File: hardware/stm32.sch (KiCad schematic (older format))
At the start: 35 parts, among them J6 PROG, Q1 PMBT3906,215, Q15 AO3400 (A09T), Q16 AO3400 (A09T), Q17 AO3400 (A09T), Q18 AO3400 (A09T), Q19 AO3400 (A09T), Q2 PMBT3906,215, Q20 AO3400 (A09T), Q3 PMBT3906,215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

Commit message: Rev5 schematic changes and pcb cleanup
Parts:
- removed Q1, Q2, Q3, Q4, Q5, Q6, Q7, Q8: PMBT3906,215, Package_TO_SOT_SMD:SOT-23, symbol Device:Q_PNP_BEC
- removed Q15, Q16, Q17, Q18, Q19, Q20: AO3400 (A09T), Package_TO_SOT_SMD:SOT-23, symbol Transistor_FET:DMN2050L
- removed R35, R36, R37, R38, R39, R40, R41, R42: 680, Resistor_SMD:R_0603_1608Metric, symbol Device:R
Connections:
- net labels added: CLK, LE, OE, SDI
- net labels removed: B1, B2, G1, G2, L1, L2, L3, L4, L5, L6, L7, L8, R1, R2, VCC
- wire segments 142 -> 69

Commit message: Finished routing rev5
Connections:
- net CLK: now also U7.26 (PB13)
- net LE: now also U7.25 (PB12)
- net OE: now also U7.27 (PB14)
- net SDI: now also U7.28 (PB15)
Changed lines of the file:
@@
 Text HLabel 4400 4200 0    50   Input ~ 0
 i2c_SDA
-Text HLabel 3650 4850 0    50   Output ~ 0
+Text HLabel 4250 4900 0    50   Output ~ 0
 OE
-Text HLabel 3650 4950 0    50   Output ~ 0
+Text HLabel 4250 4800 0    50   Output ~ 0
 CLK
-Text HLabel 3650 5050 0    50   Output ~ 0
+Text HLabel 4250 4700 0    50   Output ~ 0
+LE
+Wire Wire Line
+	4250 5000 4500 5000
+Text HLabel 4250 5000 0    50   Output ~ 0
 SDI
-Text HLabel 3650 5150 0    50   Output ~ 0
-LE
+Wire Wire Line
+	4250 4800 4500 4800
+Wire Wire Line
+	4500 4700 4250 4700
+Wire Wire Line
+	4250 4900 4500 4900
 $EndSCHEMATC

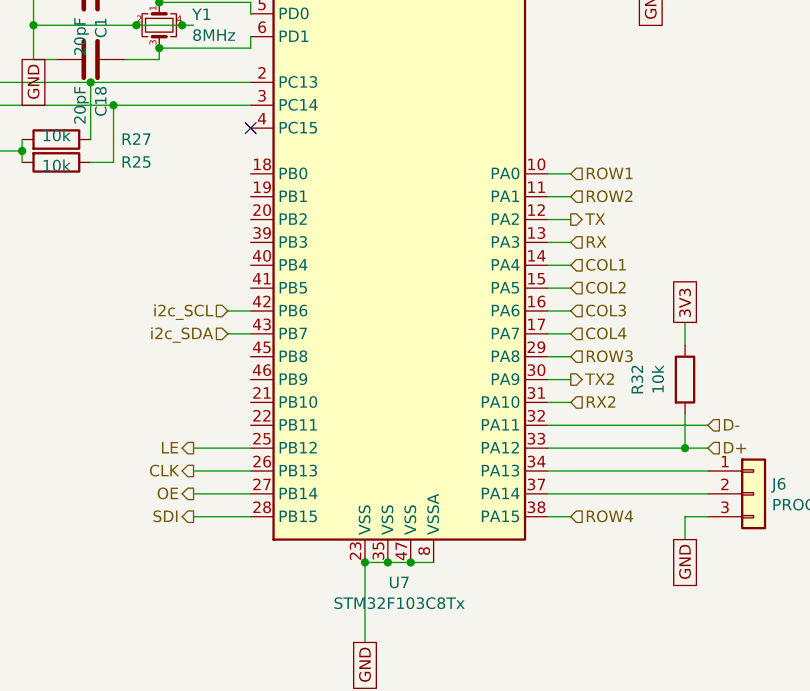
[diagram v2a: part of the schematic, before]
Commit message: UART changes
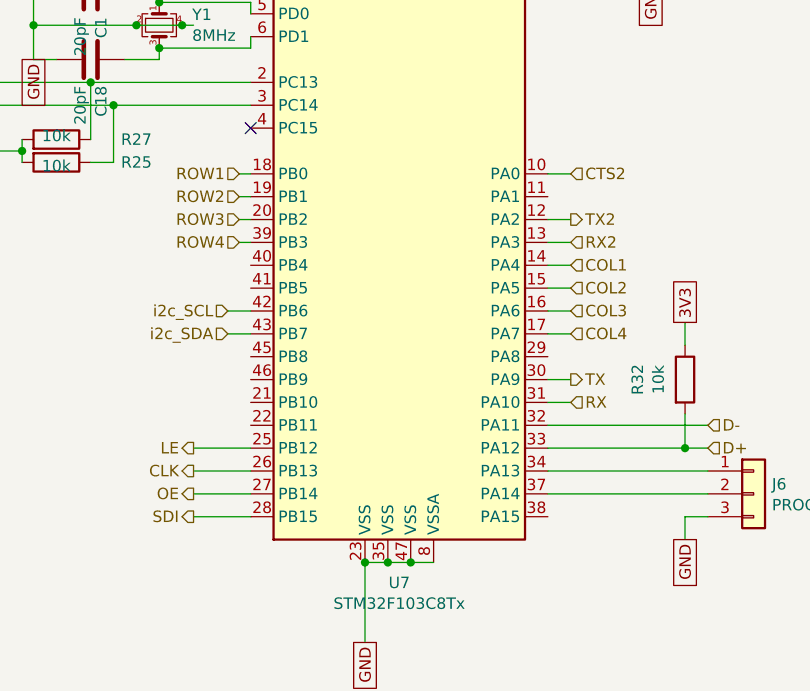
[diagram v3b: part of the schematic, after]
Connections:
- net ROW1: now also U7.18 (PB0); no longer U7.10 (PA0)
- net ROW2: now also U7.19 (PB1); no longer U7.11 (PA1)
- net ROW3: now also U7.20 (PB2); no longer U7.29 (PA8)
- net ROW4: now also U7.39 (PB3); no longer U7.38 (PA15)
- net RX: now also U7.31 (PA10); no longer U7.13 (PA3)
- net RX2: now also U7.13 (PA3); no longer U7.31 (PA10)
- net TX: now also U7.30 (PA9); no longer U7.12 (PA2)
- net TX2: now also U7.12 (PA2); no longer U7.30 (PA9)
- new net CTS2: U7.10 (PA0)
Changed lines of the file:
@@
 	4400 4100 4500 4100
 Text HLabel 5900 3700 2    50   Output ~ 0
-TX
+TX2
 Wire Wire Line
 	5900 3700 5800 3700
 Text HLabel 5900 3800 2    50   Input ~ 0
-RX
+RX2
 Wire Wire Line
 	5900 3800 5800 3800
 Text HLabel 5900 4400 2    50   Output ~ 0
-TX2
+TX
 Wire Wire Line
 	5900 4400 5800 4400
 Text HLabel 5900 4500 2    50   Input ~ 0
-RX2
+RX
 Wire Wire Line
 	5900 4500 5800 4500
-Text HLabel 5900 3500 2    50   Input ~ 0
+Text HLabel 4450 3500 0    50   Input ~ 0
 ROW1
 Text HLabel 5900 3900 2    50   Input ~ 0
@@
 Wire Wire Line
 	5900 4200 5800 4200
-Wire Wire Line
-	5900 3500 5800 3500
-Text HLabel 5900 3600 2    50   Input ~ 0
+Text HLabel 4450 3600 0    50   Input ~ 0
 ROW2
-Wire Wire Line
-	5900 3600 5800 3600
-Text HLabel 5900 4300 2    50   Input ~ 0
+Text HLabel 4450 3700 0    50   Input ~ 0
 ROW3
-Wire Wire Line
-	5900 4300 5800 4300
-Text HLabel 5900 5000 2    50   Input ~ 0
+Text HLabel 4450 3800 0    50   Input ~ 0
 ROW4
-Wire Wire Line
-	5900 5000 5800 5000
 $Comp
 L Device:Crystal_GND24_Small Y1
@@
 Wire Wire Line
 	4250 4900 4500 4900
+Wire Wire Line
+	4450 3500 4500 3500
+Wire Wire Line
+	4450 3600 4500 3600
+Wire Wire Line
+	4450 3700 4500 3700
+Wire Wire Line
+	4450 3800 4500 3800
+Text HLabel 5900 3500 2    50   Input ~ 0
+CTS2
+Wire Wire Line
+	5900 3500 5800 3500
 $EndSCHEMATC

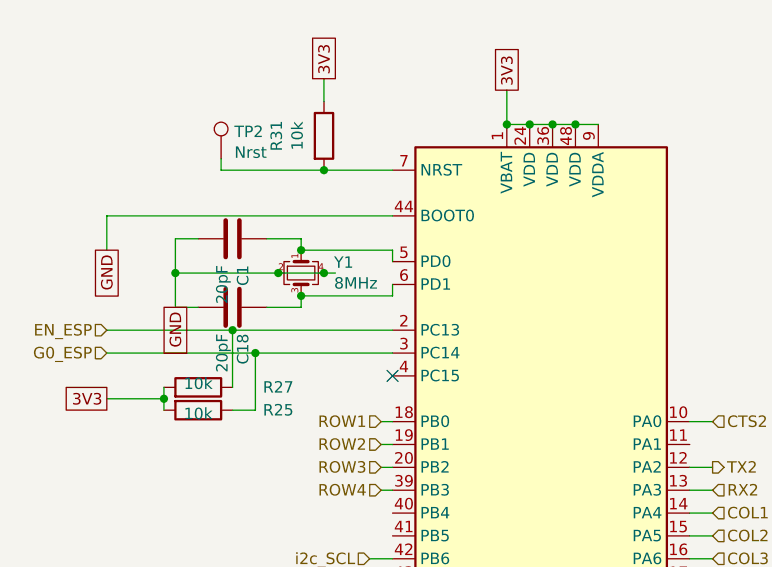
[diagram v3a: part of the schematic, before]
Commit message: Fixed BOM lines
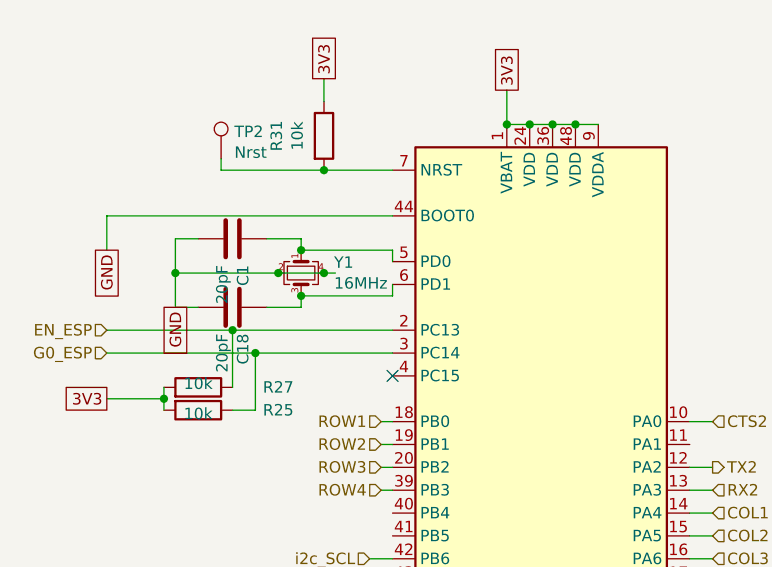
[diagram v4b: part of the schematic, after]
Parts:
- Y1: value 8MHz -> 16MHz; LCSC C280087 -> C13738
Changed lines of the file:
@@
 P 4100 2850
 F 0 "Y1" V 4054 2994 50  0000 L CNN
-F 1 "8MHz" V 4145 2994 50  0000 L CNN
+F 1 "16MHz" V 4145 2994 50  0000 L CNN
 F 2 "Crystal:Crystal_SMD_3225-4Pin_3.2x2.5mm" H 4100 2850 50  0001 C CNN
 F 3 "~" H 4100 2850 50  0001 C CNN
-F 4 "C280087" H 4100 2850 50  0001 C CNN "LCSC"
+F 4 "C13738" H 4100 2850 50  0001 C CNN "LCSC"
 	1    4100 2850
 	0    1    1    0

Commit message: Switch to tag connect for programming header
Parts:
- J6: footprint Connector_PinSocket_2.54mm:PinSocket_1x03_P2.54mm_Vertical_SMD_Pin1Left -> Connector:Tag-Connect_TC2030-IDC-NL_2x03_P1.27mm_Vertical
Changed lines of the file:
@@
 F 0 "J6" H 6780 4942 50  0000 L CNN
 F 1 "PROG" H 6780 4851 50  0000 L CNN
-F 2 "Connector_PinSocket_2.54mm:PinSocket_1x03_P2.54mm_Vertical_SMD_Pin1Left" H 6700 4900 50  0001 C CNN
+F 2 "Connector:Tag-Connect_TC2030-IDC-NL_2x03_P1.27mm_Vertical" H 6700 4900 50  0001 C CNN
 F 3 "~" H 6700 4900 50  0001 C CNN
 	1    6700 4900

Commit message: Added 5V power input to programmer header
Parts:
- J6: symbol Connector_Generic:Conn_01x03 -> Connector_Generic:Conn_01x06
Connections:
- new net VCC: J6.6 (Pin_6)
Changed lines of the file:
@@
 	4200 2850 4250 2850
 $Comp
-L Connector_Generic:Conn_01x03 J6
+L Connector_Generic:Conn_01x06 J6
 U 1 1 5E568FFD
-P 6700 4900
-F 0 "J6" H 6780 4942 50  0000 L CNN
-F 1 "PROG" H 6780 4851 50  0000 L CNN
-F 2 "Connector:Tag-Connect_TC2030-IDC-NL_2x03_P1.27mm_Vertical" H 6700 4900 50  0001 C CNN
-F 3 "~" H 6700 4900 50  0001 C CNN
-	1    6700 4900
+P 6700 5000
+F 0 "J6" H 6780 5042 50  0000 L CNN
+F 1 "PROG" H 6780 4951 50  0000 L CNN
+F 2 "Connector:Tag-Connect_TC2030-IDC-NL_2x03_P1.27mm_Vertical" H 6700 5000 50  0001 C CNN
+F 3 "~" H 6700 5000 50  0001 C CNN
+	1    6700 5000
 	1    0    0    -1
 $EndComp
@@
 Wire Wire Line
 	6500 4900 5800 4900
-Text GLabel 6400 5100 3    50   UnSpc ~ 0
+Text GLabel 6400 5000 0    50   UnSpc ~ 0
 GND
 Wire Wire Line
 	6500 5000 6400 5000
-Wire Wire Line
-	6400 5000 6400 5100
 Wire Wire Line
 	3250 2750 3250 2600
@@
 Wire Wire Line
 	5900 3500 5800 3500
+Text GLabel 6450 5300 0    50   UnSpc ~ 0
+VCC
+Wire Wire Line
+	6450 5300 6500 5300
 $EndSCHEMATC

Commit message: Final layout changes
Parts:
- added TP15, TP16: TestPoint_Small, TestPoint:TestPoint_Pad_D1.5mm, symbol Connector:TestPoint_Small
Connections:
- net at J6.1 (Pin_1), U7.34 (PA13): now also TP15.1
- net at J6.2 (Pin_2), U7.37 (PA14): now also TP16.1
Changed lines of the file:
@@
 $EndComp
 Wire Wire Line
-	5800 4800 6500 4800
+	5800 4800 6000 4800
 Wire Wire Line
-	6500 4900 5800 4900
+	6500 4900 6000 4900
 Text GLabel 6400 5000 0    50   UnSpc ~ 0
 GND
@@
 Wire Wire Line
 	6450 5300 6500 5300
+$Comp
+L Connector:TestPoint_Small TP15
+U 1 1 5ED4800E
+P 6000 4800
+F 0 "TP15" H 6048 4846 50  0000 L CNN
+F 1 "TestPoint_Small" H 6048 4755 50  0000 L CNN
+F 2 "TestPoint:TestPoint_Pad_D1.5mm" H 6200 4800 50  0001 C CNN
+F 3 "~" H 6200 4800 50  0001 C CNN
+	1    6000 4800
+	1    0    0    -1
+$EndComp
+Connection ~ 6000 4800
+Wire Wire Line
+	6000 4800 6500 4800
+$Comp
+L Connector:TestPoint_Small TP16
+U 1 1 5ED49503
+P 6000 4900
+F 0 "TP16" H 6048 4946 50  0000 L CNN
+F 1 "TestPoint_Small" H 6048 4855 50  0000 L CNN
+F 2 "TestPoint:TestPoint_Pad_D1.5mm" H 6200 4900 50  0001 C CNN
+F 3 "~" H 6200 4900 50  0001 C CNN
+	1    6000 4900
+	1    0    0    -1
+$EndComp
+Connection ~ 6000 4900
+Wire Wire Line
+	6000 4900 5800 4900
 $EndSCHEMATC
